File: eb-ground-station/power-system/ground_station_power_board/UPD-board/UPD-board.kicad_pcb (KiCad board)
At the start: 2 copper layers, 140.7 x 86.5 mm, 170 parts, among them J1 Conn_01x04, J10 PI 1827486, J2 Conn_01x03, J3 Conn_01x06, J4 Conn_01x06, J5 Conn_01x06, J6 Conn_01x06, J7 PI 1809131, J8 PI 1809131, J9 PI 1827486, Q1 DMN61D8L-LVT, Q10 DMN61D8L-LVT, Q11 SUD50P08-25L-E3, Q12 SUD50P08-25L-E3, Q13 DMN61D8L-LVT, Q14 DMN61D8L-LVT, Q15 DMN61D8L-LVT, Q16 SUD50P08-25L-E3, Q17 SUD50P08-25L-E3, Q18 DMN61D8L-LVT, Q19 SUD50P08-25L-E3, Q2 DMN61D8L-LVT, Q20 SUD50P08-25L-E3, Q21 SUD50P08-25L-E3, Q22 SUD50P08-25L-E3, Q3 DMN61D8L-LVT, Q4 SUD50P08-25L-E3, Q5 SUD50P08-25L-E3, Q6 DMN61D8L-LVT, Q7 DMN61D8L-LVT, Q8 DMN61D8L-LVT, Q9 DMN61D8L-LVT, U1 MAX7310ATE, U10 TC4427, U11 TC4427, U12 TC4427, U13 TC4427, U14 TC4427, U15 TC4427, U16 TC4427, U17 TC4427, U18 TC4427, U19 TC4427, U2 MAX7310ATE, U3 MAX7310ATE, U4 MCP9808, U5 ADS1115IDGS, U6 UA78M33, U7 U_RasPi_40pin, U8 TC4427, U9 TC4427

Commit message: More silkscreen work
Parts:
- J10, J9: footprint Connector_Phoenix_MC:PhoenixContact_MC_1,5_8-GF-3.81_1x08_P3.81mm_Horizontal_ThreadedFlange_MountHole -> oresat-footprints:J_PhoenixContact_MC_1,5_8-GF-3.81_1x08_P3.81mm_45degree_ThreadedFlange
- J7: footprint Connector_Phoenix_MC_HighVoltage:PhoenixContact_MC_1,5_8-GF-5.08_1x08_P5.08mm_Horizontal_ThreadedFlange_MountHole -> oresat-footprints:J_PhoenixContact_MC_1,5_8-GF-5.08_1x08_P5.08mm_Horizontal_ThreadedFlange
- J8: value PI 1809131 -> PI 1827923; footprint Connector_Phoenix_MC_HighVoltage:PhoenixContact_MC_1,5_8-GF-5.08_1x08_P5.08mm_Horizontal_ThreadedFlange_MountHole -> Connector_Phoenix_MC:PhoenixContact_MC_1,5_8-GF-3.81_1x08_P3.81mm_Horizontal_ThreadedFlange
- JP1, JP10, JP11, JP12, JP13, JP2, JP3, JP4, JP5, JP6, JP7, JP8, JP9: footprint Jumper:SolderJumper-3_P1.3mm_Bridged12_Pad1.0x1.5mm -> oresat-footprints:SolderJumper-3_P1.3mm_Bridged12_Pad1.0x1.5mm
- U1, U2, U3: footprint Package_SO:TSSOP-16_4.4x5mm_P0.65mm -> oresat-footprints:TSSOP-16_4.4x5mm_P0.65mm
- moved RN7 20.9 mm to (132.3, 96.0)
- moved D10 15.9 mm to (146.5, 91.2)
- moved D3 15.9 mm to (125.1, 91.2)
- moved D5 15.9 mm to (131.2, 91.2)
- moved D6 15.9 mm to (134.3, 91.2)
- moved D7 15.9 mm to (137.3, 91.2)
- moved D8 15.9 mm to (140.4, 91.2)
- moved D4 15.9 mm to (128.2, 91.2)
- moved D9 15.9 mm to (143.4, 91.2)
- moved RN8 13.0 mm to (140.9, 96.1)
- moved J8 4.99 mm to (165.5, 131.6)
- moved C1 2.52 mm to (122.4, 91.1), turned to 180 degrees
- moved C3 2.31 mm to (131.9, 59.2), turned to 180 degrees
- moved JP10 2.24 mm to (169.2, 67.7)
- moved C4 1.84 mm to (169.2, 69.7)
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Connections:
- C11 pad 1: GND -> +5V
- C11 pad 2: +5V -> GND
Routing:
- net GND: track 87.2 -> 130.2 mm, vias 302 -> 310
- net GNDA: track 48.6 -> 9.60 mm
- net CTL_A4: track 49.3 -> 36.8 mm, vias 3 -> 4
- net CTL_A0: track 46.7 -> 34.5 mm, vias 4 -> 5
- net CTL_A1: track 46.3 -> 34.5 mm, vias 4 -> 5
- net CTL_C1: track 45.4 -> 34.1 mm, vias 4 -> 5
- net CTL_A2: track 58.2 -> 47.2 mm, vias 4 -> 5
- net CTL_C2: track 39.3 -> 29.2 mm, vias 2 -> 3
- net CTL_A3: track 54.2 -> 45.4 mm, vias 4 -> 6
- net CTL_C3: track 40.1 -> 31.5 mm, vias 2 -> 3
- net CTL_A5: track 47.0 -> 40.0 mm, vias 3 -> 4
- net Net-(D6-Pad2): track 9.71 -> 3.45 mm
- net Net-(D5-Pad2): track 7.36 -> 3.77 mm
- net Net-(D7-Pad2): track 7.53 -> 4.83 mm
- net CTL_C0: track 35.9 -> 33.2 mm
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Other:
- board text added: "0"
- board text added: "1"
- board text added: "2"
- board text added: "3"
- board text added: "4"
- board text added: "5"
- board text added: "6"
- board text added: "7"
- board text added: "A0"
- board text added: "A1"
- board text added: "A2"
- board text added: "A3"
- board text added: "AG"
- board text added: "Analog"
- board text added: "Analog Inputs"
- board text added: "Bank"
- board text added: "Bank C"
- board text added: "agnd"
- board text removed: "gnda"

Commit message: Added PDFs and PNGs of the board
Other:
- board text added: "B.Cu"
- board text added: "B.Silk"
- board text added: "F.Cu"
- board text added: "F.Silk"
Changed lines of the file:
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@@
   (gr_rect (start 190.7286 87.7062) (end 148.209 53.721) (layer "F.SilkS") (width 0.125) (fill none))
   (gr_rect (start 74.8792 53.1876) (end 215.5952 139.7254) (layer "Edge.Cuts") (width 0.1) (fill none))
+  (gr_text "F.Cu" (at 214.4776 183.007) (layer "F.Cu")
+    (effects (font (size 1.5 1.5) (thickness 0.3)))
+  )
+  (gr_text "B.Cu" (at 214.376 186.0042) (layer "B.Cu")
+    (effects (font (size 1.5 1.5) (thickness 0.3)))
+  )
   (gr_text "Designed by Benjamin Crall" (at 152.273 136.779) (layer "B.Cu")
     (effects (font (size 1.5 1.5) (thickness 0.3)) (justify mirror))
+  )
+  (gr_text "B.Silk" (at 222.4532 185.9788) (layer "B.SilkS")
+    (effects (font (size 1.5 1.5) (thickness 0.3)))
   )
   (gr_text "2" (at 131.2418 89.0524) (layer "F.SilkS")
@@
     (effects (font (size 1 1) (thickness 0.15)))
   )
+  (gr_text "F.Silk" (at 222.5548 183.0324) (layer "F.SilkS")
+    (effects (font (size 1.5 1.5) (thickness 0.3)))
+  )
   (gr_text "4" (at 182.6006 104.521) (layer "F.SilkS")

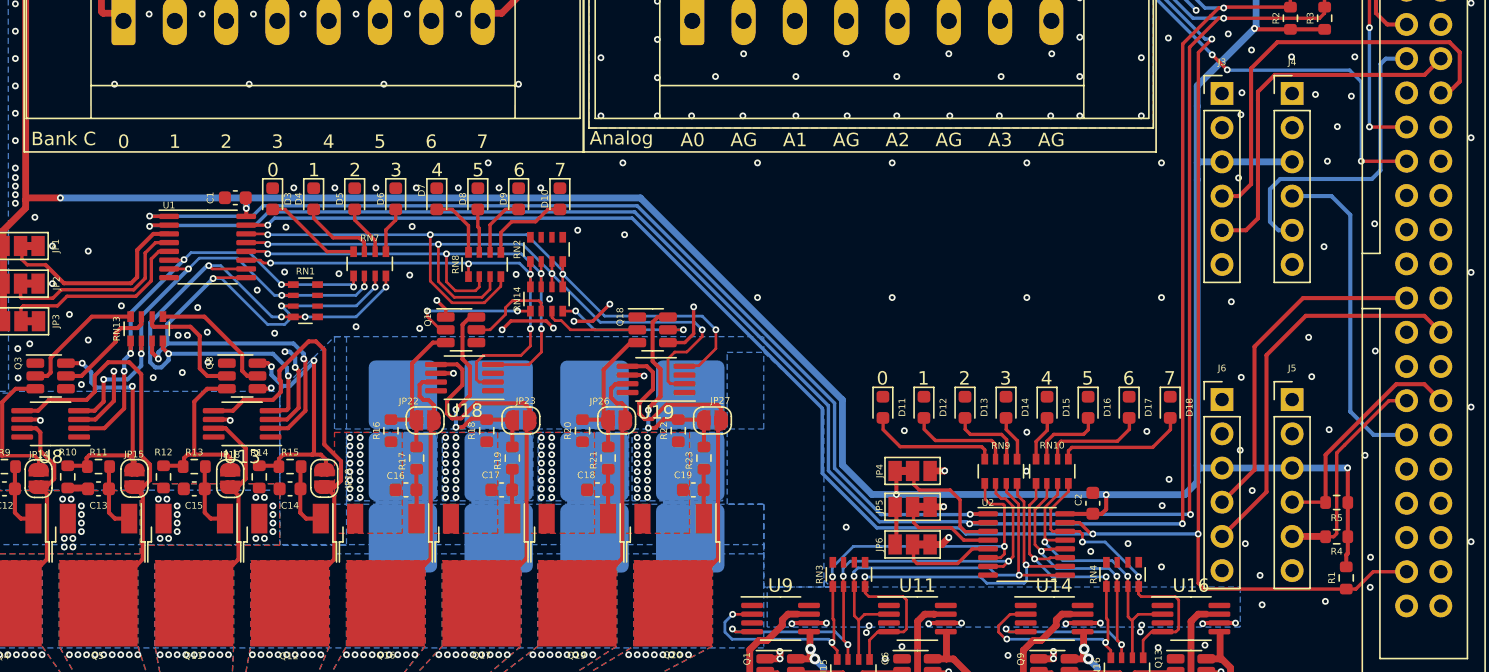
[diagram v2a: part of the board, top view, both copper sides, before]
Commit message: Fixed ~IO_RESET RasPi pin and improved silkscreen
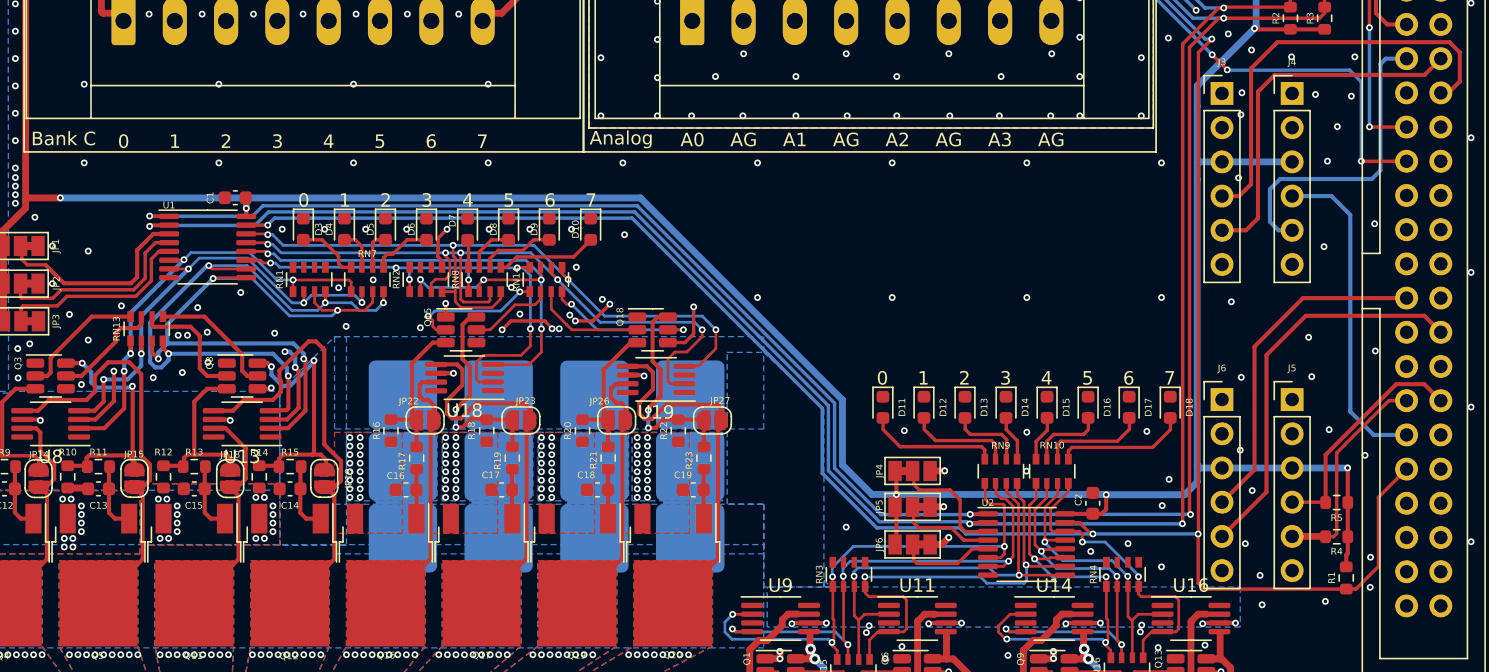
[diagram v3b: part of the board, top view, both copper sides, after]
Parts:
- moved RN2 9.24 mm to (136.5, 97.2)
- moved D10 3.21 mm to (148.7, 93.4)
- moved D3 3.21 mm to (127.4, 93.4)
- moved D4 3.21 mm to (130.5, 93.4)
- moved D5 3.21 mm to (133.5, 93.4)
- moved D6 3.21 mm to (136.6, 93.4)
- moved D7 3.21 mm to (139.6, 93.4)
- moved D8 3.21 mm to (142.6, 93.4)
- moved D9 3.21 mm to (145.7, 93.4)
- moved RN1 1.60 mm to (127.8, 97.2), turned to -90 degrees
- moved RN14 1.45 mm to (145.4, 97.2)
- moved RN7 1.18 mm to (132.2, 97.2)
- moved RN8 1.12 mm to (140.9, 97.2)
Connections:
- U7 pad 31: unconnected-(U7-Pad31) -> ~{IO_RESET}
- U7 pad 37: ~{IO_RESET} -> unconnected-(U7-Pad37)
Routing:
- net ~{IO_RESET}: track 210.0 -> 216.1 mm
- net CTL_A5: track 40.0 -> 44.6 mm, vias 4 -> 5
- net Net-(D4-Pad2): track 5.84 -> 3.06 mm
- net Net-(D7-Pad2): track 4.83 -> 2.08 mm
- net GND: track 130.2 -> 132.8 mm, vias 310 -> 314
- net Net-(D3-Pad2): track 7.31 -> 4.72 mm
- net CTL_A7: track 54.7 -> 52.8 mm
- net CTL_A4: track 36.8 -> 38.5 mm, vias 4 -> 6
- net CTL_A6: track 53.4 -> 54.8 mm, vias 4 -> 5
- net MOS_A6: track 7.18 -> 8.33 mm
- net Net-(D6-Pad2): track 3.45 -> 4.46 mm
- net Net-(D9-Pad2): track 4.64 -> 5.64 mm
- net MOS_A7: track 10.7 -> 11.7 mm
- net Net-(D10-Pad2): track 6.57 -> 7.52 mm
- net Net-(D5-Pad2): track 3.77 -> 2.87 mm
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
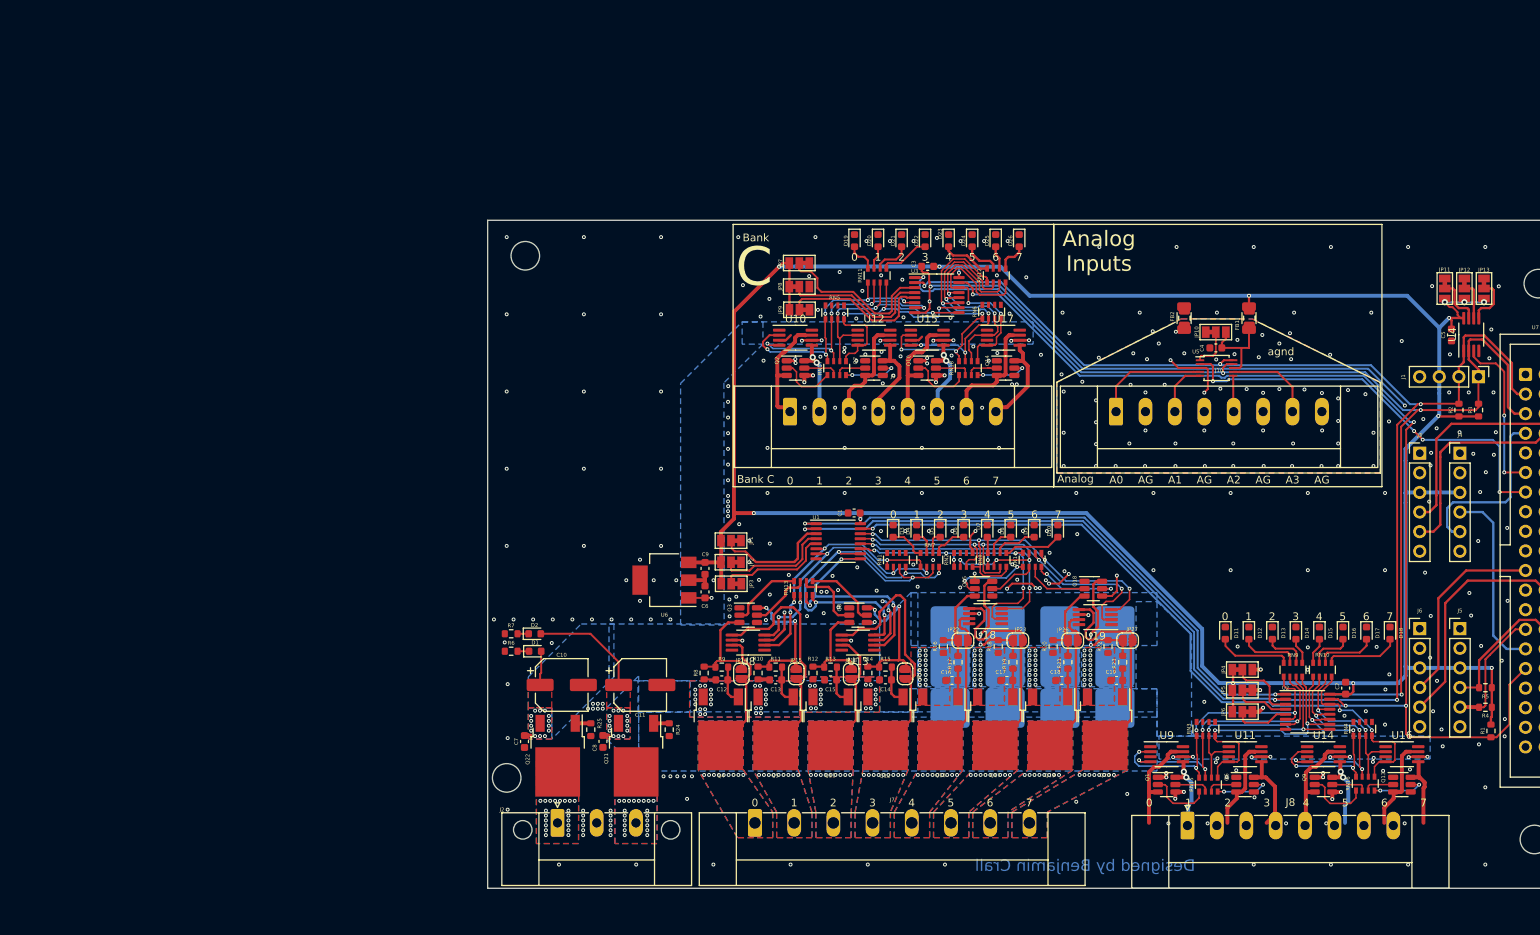
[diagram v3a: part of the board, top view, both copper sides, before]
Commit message: Fixed some issues and added propper power input connector
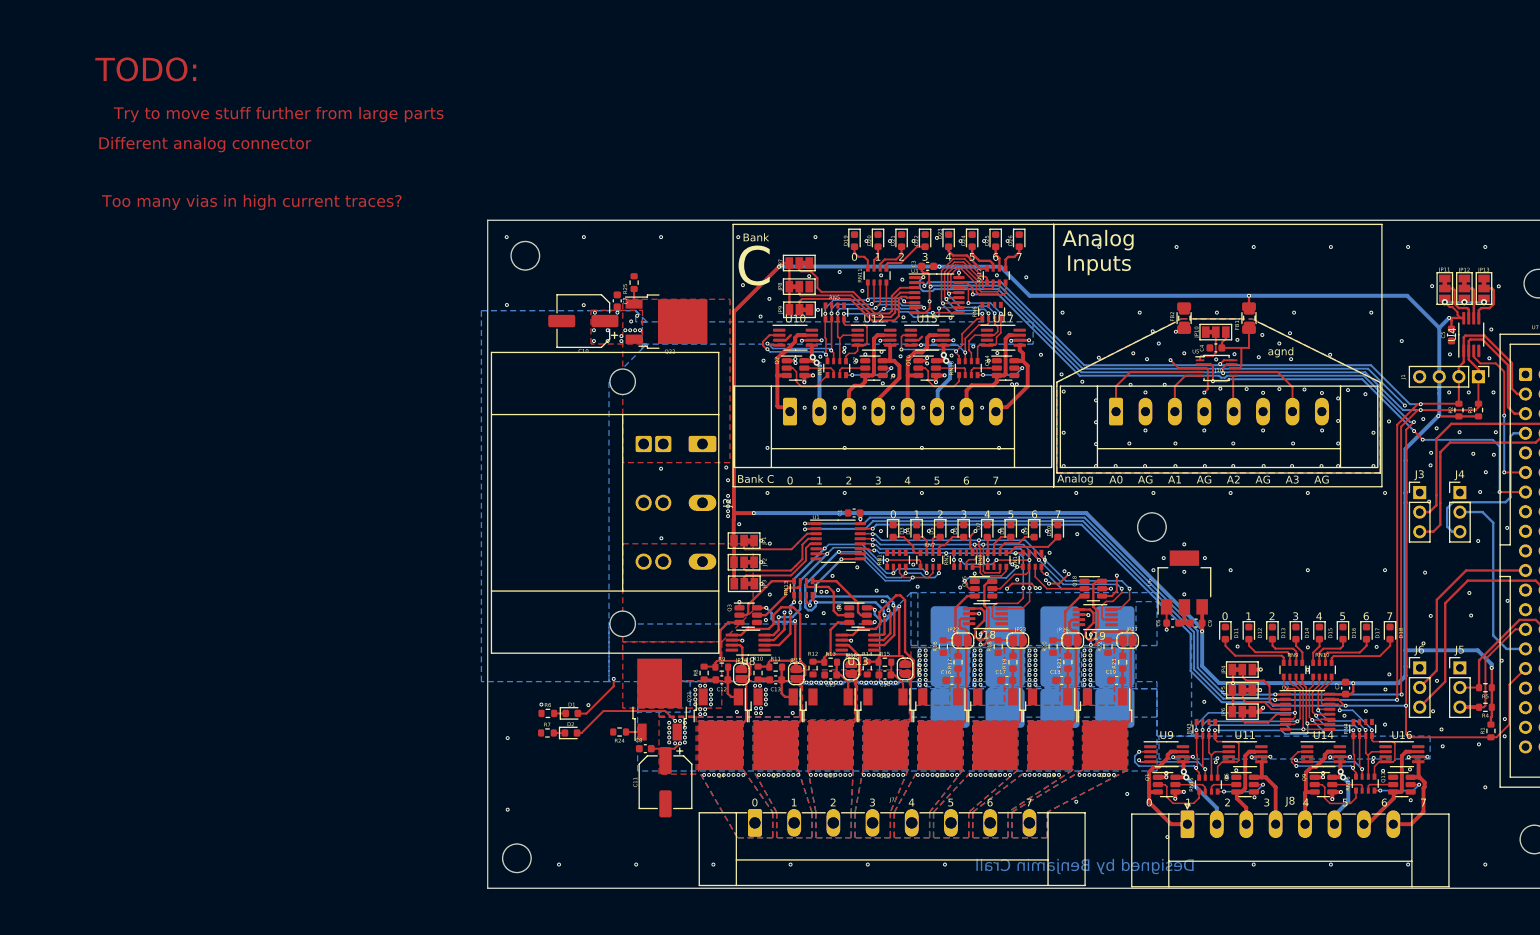
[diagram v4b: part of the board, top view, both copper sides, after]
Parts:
- added H5: MountingHole, oresat-footprints:H-MCMASTER-94100A150, F.Cu at (160.9, 92.9)
- J2: value Conn_01x03 -> PC 1720806; footprint Connector_Phoenix_MC_HighVoltage:PhoenixContact_MC_1,5_3-GF-5.08_1x03_P5.08mm_Horizontal_ThreadedFlange_MountHole -> oresat-footprints:PhoenixContact_GMSTBA_2,5_3-G-7,62_1x03_P7.62mm_Horizontal
- J3, J4, J5, J6: value Conn_01x06 -> Conn_01x03; footprint Connector_PinHeader_2.54mm:PinHeader_1x06_P2.54mm_Vertical -> Connector_PinHeader_2.54mm:PinHeader_1x03_P2.54mm_Vertical
- J7: value PI 1809131 -> PI 1924143
- J8: footprint Connector_Phoenix_MC:PhoenixContact_MC_1,5_8-GF-3.81_1x08_P3.81mm_Horizontal_ThreadedFlange -> oresat-footprints:PhoenixContact_MC_1,5_8-GF-3.81_1x08_P3.81mm_Horizontal_ThreadedFlange
- moved U6 67.4 mm to (165.1, 100.1), turned to 90 degrees
- moved C9 64.0 mm to (166.7, 105.4), turned to 180 degrees
- moved C6 60.7 mm to (163.6, 105.4), turned to 0 degrees
- moved C7 58.3 mm to (91.7, 63.6), turned to 90 degrees
- moved R25 58.2 mm to (93.9, 61.3), turned to -90 degrees
- moved Q22 58.0 mm to (98.0, 66.3), turned to 0 degrees
- moved J2 52.6 mm to (102.7, 82.2), turned to -90 degrees
- moved C10 47.2 mm to (87.3, 66.2), turned to 180 degrees
- moved D2 13.7 mm to (85.7, 119.6)
- moved R7 13.7 mm to (82.6, 119.6)
- moved C11 13.0 mm to (97.9, 126.0), turned to -90 degrees
- moved H1 10.5 mm to (78.7, 135.8)
- moved D1 9.35 mm to (85.8, 117.1)
- moved R6 9.35 mm to (82.7, 117.1)
- moved Q21 7.89 mm to (97.2, 115.3), turned to 90 degrees
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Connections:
- J3 pad 2: unconnected-(J3-Pad2) -> RX0
- J3 pad 3: +3V3 -> TX0
- J4 pad 2: unconnected-(J4-Pad2) -> RX3
- J4 pad 3: +3V3 -> TX3
- J5 pad 2: unconnected-(J5-Pad2) -> RX2
- J5 pad 3: +3V3 -> TX2
- J6 pad 2: unconnected-(J6-Pad2) -> RX4
- J6 pad 3: +3V3 -> TX4
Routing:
- net +3V3: track 395.2 -> 382.1 mm, vias 14 -> 15
- net Net-(JP1-Pad2): track 15.4 -> 11.2 mm
- net OUT_B0: track 12.7 -> 16.2 mm
- net OUT_B7: track 9.29 -> 12.4 mm
- net +5V: track 18.4 -> 21.5 mm, vias 38 -> 40
- net +12V: track 31.8 -> 33.7 mm, vias 50 -> 51
- net Net-(JP2-Pad2): track 14.8 -> 13.0 mm
- net Net-(JP3-Pad2): track 14.6 -> 12.8 mm
- net OUT_B6: track 11.6 -> 13.1 mm
- net OUT_B1: track 10.6 -> 12.0 mm
- net Net-(JP19-Pad1): track 19.6 -> 18.8 mm
- net GND: track 132.8 -> 133.6 mm, vias 314 -> 255
- net OUT_B5: track 10.6 -> 11.4 mm
- net Net-(JP18-Pad1): track 13.4 -> 12.7 mm
- net OUT_A2: track 16.9 -> 17.5 mm
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- removed copper zone on B.Cu, net 12V_RAW
- removed copper zone on B.Cu, net 5v_RAW
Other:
- board text added: "Different analog connector"
- board text added: "TODO:"
- board text added: "Too many vias in high current traces?"
- board text added: "Try to move stuff further from large parts"
